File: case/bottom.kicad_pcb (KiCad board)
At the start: 2 copper layers, 137.8 x 95.7 mm, 9 parts

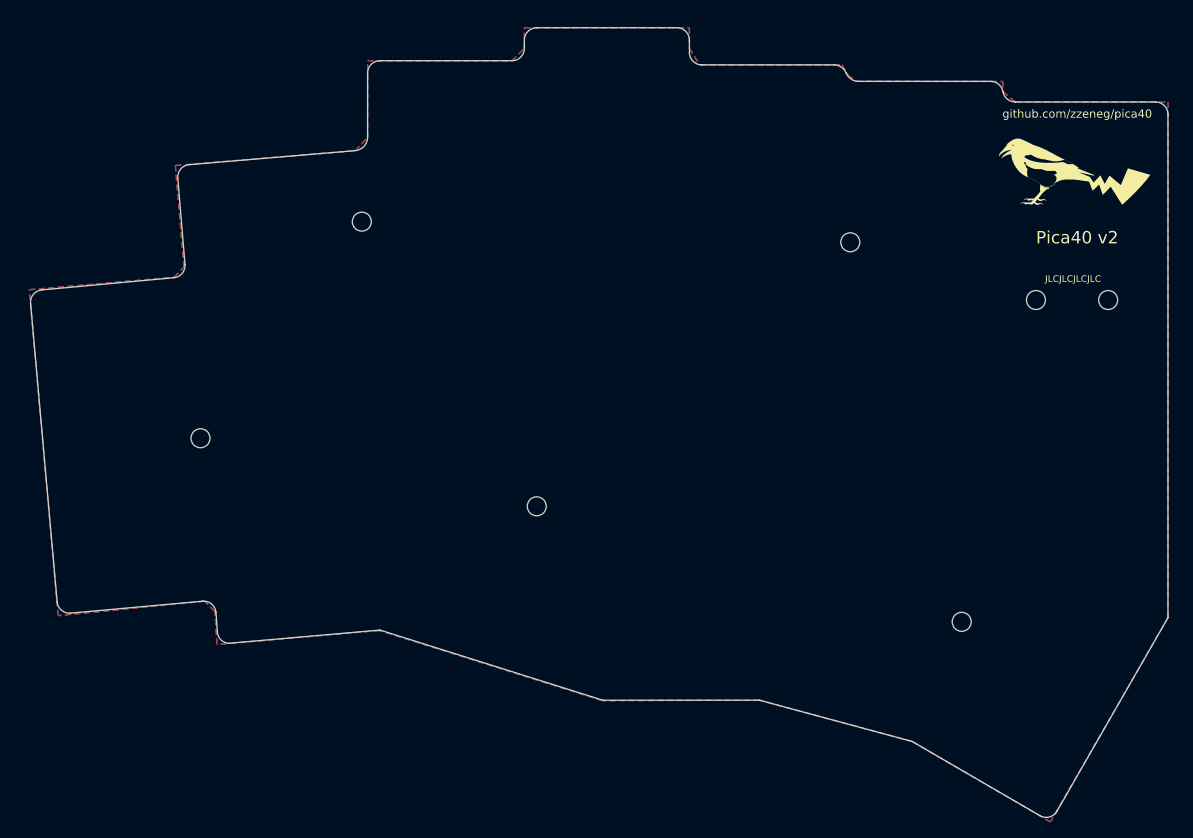
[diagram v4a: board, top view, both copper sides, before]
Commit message: remove zones from bottom to prevent shorting
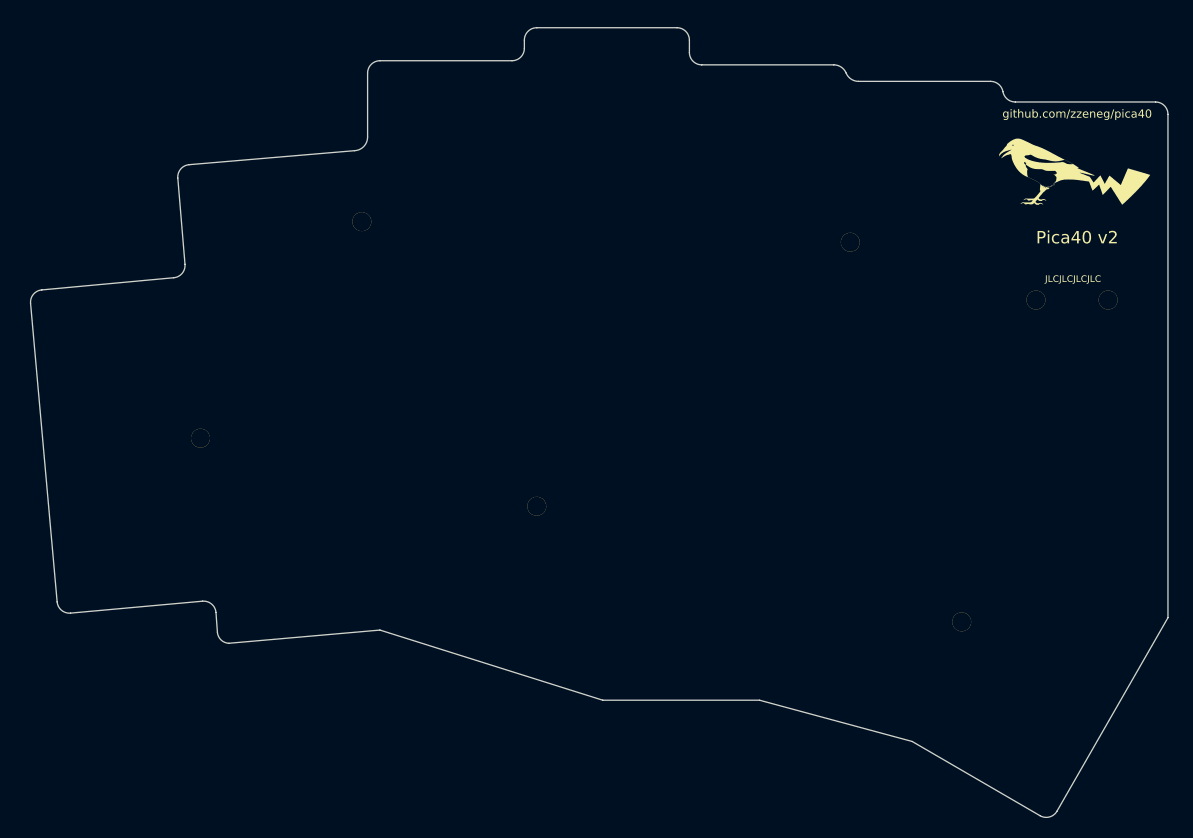
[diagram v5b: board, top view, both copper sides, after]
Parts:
- H1, H2, H3, H4, H5, H6, H7: footprint kbd:thread_m2 -> kbd:M2_Threads_v2
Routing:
- removed copper zone on B.Cu, net (none)
- removed copper zone on F.Cu, net (none)
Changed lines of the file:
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@@
       ) (layer "F.SilkS") (width 0) (fill solid))
   )
-  (footprint "kbd:thread_m2" (layer "F.Cu")
+  (footprint "kbd:M2_Threads_v2" (layer "F.Cu")
     (at 90.75 100.81066 5)
     (descr "Mounting Hole 2.2mm, no annular, M2")
@@
       (effects (font (size 1 1) (thickness 0.15)))
     )
-    (pad "" np_thru_hole circle locked (at 0 0 5) (size 2.3 2.3) (drill 2.3) (layers *.Cu *.Mask))
+    (pad "" thru_hole circle locked (at 0 0 5) (size 2.3 2.3) (drill 2.3) (layers *.Cu *.Mask))
   )
-  (footprint "kbd:thread_m2" (layer "F.Cu")
+  (footprint "kbd:M2_Threads_v2" (layer "F.Cu")
     (at 192 84.06066)
     (descr "Mounting Hole 2.2mm, no annular, M2")
@@
     (property "Sheetfile" "full.kicad_sch")
     (property "Sheetname" "")
-    (attr exclude_from_pos_files)
+    (attr exclude_from_pos_files exclude_from_bom)
     (fp_text reference "H6" (at -0.95 -0.55) (layer "F.Fab") hide
       (effects (font (size 1 1) (thickness 0.15)))
@@
       (effects (font (size 1 1) (thickness 0.15)))
     )
-    (pad "" np_thru_hole circle locked (at 0 0) (size 2.3 2.3) (drill 2.3) (layers *.Cu *.Mask))
+    (pad "" thru_hole circle locked (at 0 0) (size 2.3 2.3) (drill 2.3) (layers *.Cu *.Mask))
   )
-  (footprint "kbd:thread_m2" (layer "F.Cu")
+  (footprint "kbd:M2_Threads_v2" (layer "F.Cu")
     (at 110.3 74.56066)
     (descr "Mounting Hole 2.2mm, no annular, M2")
@@
       (effects (font (size 1 1) (thickness 0.15)))
     )
-    (pad "" np_thru_hole circle locked (at 0 0) (size 2.3 2.3) (drill 2.3) (layers *.Cu *.Mask))
+    (pad "" thru_hole circle locked (at 0 0) (size 2.3 2.3) (drill 2.3) (layers *.Cu *.Mask))
   )
-  (footprint "kbd:thread_m2" (layer "F.Cu")
+  (footprint "kbd:M2_Threads_v2" (layer "F.Cu")
     (at 131.5 109.06066)
     (descr "Mounting Hole 2.2mm, no annular, M2")
@@
       (effects (font (size 1 1) (thickness 0.15)))
     )
-    (pad "" np_thru_hole circle locked (at 0 0) (size 2.3 2.3) (drill 2.3) (layers *.Cu *.Mask))
+    (pad "" thru_hole circle locked (at 0 0) (size 2.3 2.3) (drill 2.3) (layers *.Cu *.Mask))
   )
-  (footprint "kbd:thread_m2" (layer "F.Cu")
+  (footprint "kbd:M2_Threads_v2" (layer "F.Cu")
     (at 200.75 84.06066)
     (descr "Mounting Hole 2.2mm, no annular, M2")
@@
     (property "Sheetfile" "full.kicad_sch")
     (property "Sheetname" "")
-    (attr exclude_from_pos_files)
+    (attr exclude_from_pos_files exclude_from_bom)
     (fp_text reference "H7" (at -0.95 -0.55) (layer "F.Fab") hide
       (effects (font (size 1 1) (thickness 0.15)))
@@
       (effects (font (size 1 1) (thickness 0.15)))
     )
-    (pad "" np_thru_hole circle locked (at 0 0) (size 2.3 2.3) (drill 2.3) (layers *.Cu *.Mask))
+    (pad "" thru_hole circle locked (at 0 0) (size 2.3 2.3) (drill 2.3) (layers *.Cu *.Mask))
   )
-  (footprint "kbd:thread_m2" (layer "F.Cu")
+  (footprint "kbd:M2_Threads_v2" (layer "F.Cu")
     (at 183 123.06066)
     (descr "Mounting Hole 2.2mm, no annular, M2")
@@
       (effects (font (size 1 1) (thickness 0.15)))
     )
-    (pad "" np_thru_hole circle locked (at 0 0) (size 2.3 2.3) (drill 2.3) (layers *.Cu *.Mask))
+    (pad "" thru_hole circle locked (at 0 0) (size 2.3 2.3) (drill 2.3) (layers *.Cu *.Mask))
   )
-  (footprint "kbd:thread_m2" (layer "F.Cu")
+  (footprint "kbd:M2_Threads_v2" (layer "F.Cu")
     (at 169.5 77.06066)
     (descr "Mounting Hole 2.2mm, no annular, M2")
@@
       (effects (font (size 1 1) (thickness 0.15)))
     )
-    (pad "" np_thru_hole circle locked (at 0 0) (size 2.3 2.3) (drill 2.3) (layers *.Cu *.Mask))
+    (pad "" thru_hole circle locked (at 0 0) (size 2.3 2.3) (drill 2.3) (layers *.Cu *.Mask))
   )
   (footprint "pica:logo" (layer "B.Cu")
@@
     (effects (font (size 1 1) (thickness 0.15)))
   )
-  (zone (net 0) (net_name "") (layers F&B.Cu) (hatch edge 0.508)
-    (connect_pads (clearance 0.508))
-    (min_thickness 0.254) (filled_areas_thickness no)
-    (fill yes (thermal_gap 0.508) (thermal_bridge_width 0.508) (island_removal_mode 1) (island_area_min 0))
-    (polygon
-      (pts
-        (xy 150 53.56066)
-        (xy 151.249191 55.56066)
-        (xy 168.5 55.56066)
-        (xy 169.25 56.81066)
-        (xy 170.25 57.56066)
-        (xy 187.999191 57.57255)
-        (xy 188 58.81066)
-        (xy 189.5 60.06066)
-        (xy 208 60.06066)
-        (xy 208 122.56066)
-        (xy 193.75 147.31066)
-        (xy 177 137.56066)
-        (xy 158.5 132.56066)
-        (xy 139.45 132.61066)
-        (xy 112.45 124.11066)
-        (xy 92.75 125.81066)
-        (xy 92.5 121.81066)
-        (xy 91.25 120.56066)
-        (xy 73.5 122.31066)
-        (xy 70 82.81066)
-        (xy 87.55439 81.297127)
-        (xy 88.75 80.06066)
-        (xy 87.7 67.76066)
-        (xy 109.5 65.96066)
-        (xy 111 64.36066)
-        (xy 111 55.06066)
-        (xy 128.5 55.06066)
-        (xy 130 53.56066)
-        (xy 130 51.06066)
-        (xy 150 51.06066)
-      )
-    )
-  )
 )

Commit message: update pcb
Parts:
- H1, H2, H3, H4, H5, H6, H7: footprint kbd:M2_Threads_v2 -> zzkeeb:Hole_M2
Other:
- board text removed: "JLCJLCJLCJLC"
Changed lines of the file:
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@@
       (disableapertmacros false)
       (usegerberextensions true)
-      (usegerberattributes false)
+      (usegerberattributes true)
       (usegerberadvancedattributes false)
       (creategerberjobfile false)
@@
       (psnegative false)
       (psa4output false)
-      (plotreference true)
+      (plotreference false)
       (plotvalue false)
       (plotinvisibletext false)
@@
       ) (layer "F.SilkS") (width 0) (fill solid))
   )
-  (footprint "kbd:M2_Threads_v2" (layer "F.Cu")
+  (footprint "zzkeeb:Hole_M2" (layer "F.Cu")
     (at 90.75 100.81066 5)
     (descr "Mounting Hole 2.2mm, no annular, M2")
@@
       (effects (font (size 1 1) (thickness 0.15)))
     )
-    (pad "" thru_hole circle locked (at 0 0 5) (size 2.3 2.3) (drill 2.3) (layers *.Cu *.Mask))
+    (pad "" np_thru_hole circle (at 0 0 5) (size 2.3 2.3) (drill 2.3) (layers *.Cu *.Mask))
   )
-  (footprint "kbd:M2_Threads_v2" (layer "F.Cu")
+  (footprint "zzkeeb:Hole_M2" (layer "F.Cu")
     (at 192 84.06066)
     (descr "Mounting Hole 2.2mm, no annular, M2")
@@
       (effects (font (size 1 1) (thickness 0.15)))
     )
-    (pad "" thru_hole circle locked (at 0 0) (size 2.3 2.3) (drill 2.3) (layers *.Cu *.Mask))
+    (pad "" np_thru_hole circle (at 0 0) (size 2.3 2.3) (drill 2.3) (layers *.Cu *.Mask))
   )
-  (footprint "kbd:M2_Threads_v2" (layer "F.Cu")
+  (footprint "zzkeeb:Hole_M2" (layer "F.Cu")
     (at 110.3 74.56066)
     (descr "Mounting Hole 2.2mm, no annular, M2")
@@
       (effects (font (size 1 1) (thickness 0.15)))
     )
-    (pad "" thru_hole circle locked (at 0 0) (size 2.3 2.3) (drill 2.3) (layers *.Cu *.Mask))
+    (pad "" np_thru_hole circle (at 0 0) (size 2.3 2.3) (drill 2.3) (layers *.Cu *.Mask))
   )
-  (footprint "kbd:M2_Threads_v2" (layer "F.Cu")
+  (footprint "zzkeeb:Hole_M2" (layer "F.Cu")
     (at 131.5 109.06066)
     (descr "Mounting Hole 2.2mm, no annular, M2")
@@
       (effects (font (size 1 1) (thickness 0.15)))
     )
-    (pad "" thru_hole circle locked (at 0 0) (size 2.3 2.3) (drill 2.3) (layers *.Cu *.Mask))
+    (pad "" np_thru_hole circle (at 0 0) (size 2.3 2.3) (drill 2.3) (layers *.Cu *.Mask))
   )
-  (footprint "kbd:M2_Threads_v2" (layer "F.Cu")
+  (footprint "zzkeeb:Hole_M2" (layer "F.Cu")
     (at 200.75 84.06066)
     (descr "Mounting Hole 2.2mm, no annular, M2")
@@
       (effects (font (size 1 1) (thickness 0.15)))
     )
-    (pad "" thru_hole circle locked (at 0 0) (size 2.3 2.3) (drill 2.3) (layers *.Cu *.Mask))
+    (pad "" np_thru_hole circle (at 0 0) (size 2.3 2.3) (drill 2.3) (layers *.Cu *.Mask))
   )
-  (footprint "kbd:M2_Threads_v2" (layer "F.Cu")
+  (footprint "zzkeeb:Hole_M2" (layer "F.Cu")
     (at 183 123.06066)
     (descr "Mounting Hole 2.2mm, no annular, M2")
@@
       (effects (font (size 1 1) (thickness 0.15)))
     )
-    (pad "" thru_hole circle locked (at 0 0) (size 2.3 2.3) (drill 2.3) (layers *.Cu *.Mask))
+    (pad "" np_thru_hole circle (at 0 0) (size 2.3 2.3) (drill 2.3) (layers *.Cu *.Mask))
   )
-  (footprint "kbd:M2_Threads_v2" (layer "F.Cu")
+  (footprint "zzkeeb:Hole_M2" (layer "F.Cu")
     (at 169.5 77.06066)
     (descr "Mounting Hole 2.2mm, no annular, M2")
@@
       (effects (font (size 1 1) (thickness 0.15)))
     )
-    (pad "" thru_hole circle locked (at 0 0) (size 2.3 2.3) (drill 2.3) (layers *.Cu *.Mask))
+    (pad "" np_thru_hole circle (at 0 0) (size 2.3 2.3) (drill 2.3) (layers *.Cu *.Mask))
   )
   (footprint "pica:logo" (layer "B.Cu")
@@
     (effects (font (size 1 1) (thickness 0.15)) (justify mirror))
   )
-  (gr_text "JLCJLCJLCJLC" (at 196.5 81.5) (layer "F.SilkS")
-    (effects (font (size 0.8 0.8) (thickness 0.15)))
-  )
   (gr_text "Pica40 v2" (at 197 76.5) (layer "F.SilkS")

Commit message: update bottom
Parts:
- H1, H2, H3, H4, H5, H6, H7: footprint zzkeeb:Hole_M2 -> zzkeeb:Hole_M2-cutout
- moved H1 0.06 mm to (110.3, 74.5)
- moved H2 0.06 mm to (183.0, 123.0)
- moved H3 0.06 mm to (90.8, 100.8)
- moved H4 0.06 mm to (131.5, 109.0)
- moved H5 0.06 mm to (169.5, 77.0)
- moved H6 0.06 mm to (192.0, 84.0)
- moved H7 0.06 mm to (200.8, 84.0)
